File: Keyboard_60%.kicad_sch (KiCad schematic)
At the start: 24 parts, among them J3 Prog_conn, U3 NRF52833-QDAA-R7, Y1 32MHz, Y2 32.768kHz

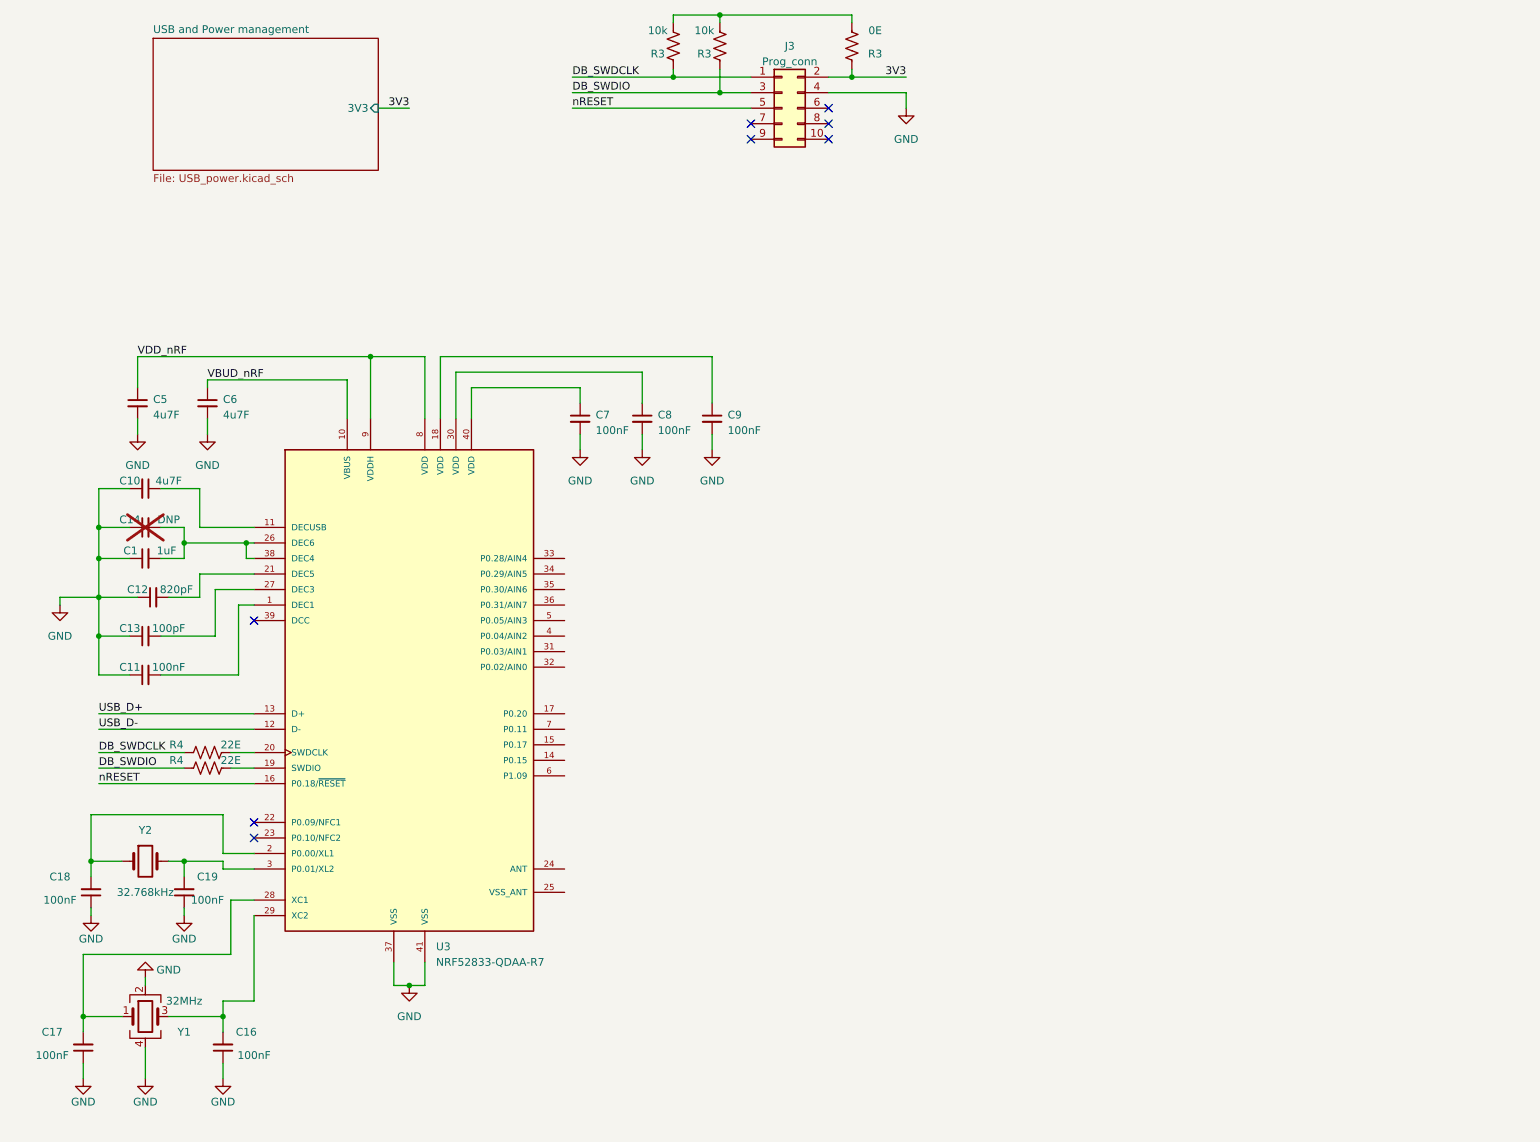
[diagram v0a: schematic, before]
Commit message: added seitch matrix to schematic
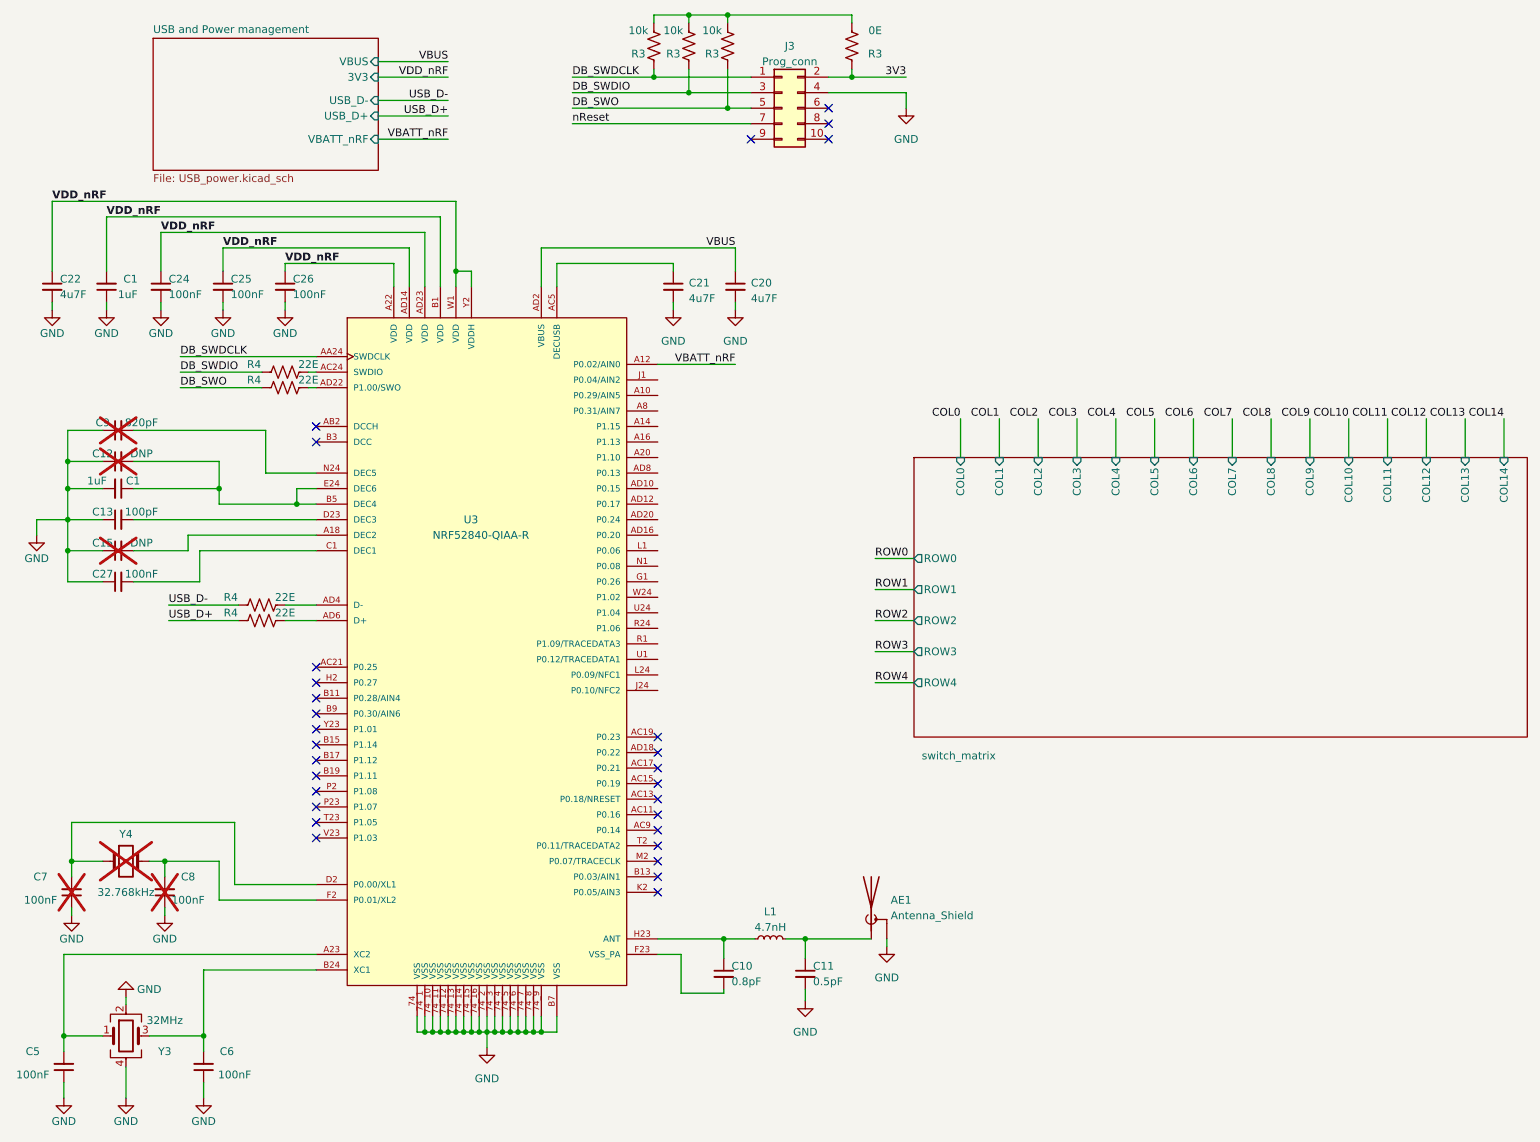
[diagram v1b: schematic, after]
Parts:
- removed C1: 1uF, symbol Device:C_Small
- removed C14: DNP, symbol keyboard:C_Small
- removed C16, C17, C18, C19: 100nF, symbol keyboard:C_Small
- removed R4 (x2): 22E, symbol keyboard:R_US
- removed U3: NRF52833-QDAA-R7, QFN40P500X500X90-41N, symbol keyboard:NRF52833-QDAA-R7
- removed Y1: 32MHz, symbol keyboard:Crystal_GND24
- removed Y2: 32.768kHz, symbol keyboard:Crystal
- added AE1: Antenna_Shield, symbol keyboard:Antenna_Shield
- added C1 (x2): 1uF, symbol Device:C_Small
- added C15: DNP, symbol keyboard:C_Small
- added C20, C21, C22: 4u7F, symbol keyboard:C_Small
- added C24, C25, C26, C27: 100nF, symbol keyboard:C_Small
- added L1: 4.7nH, symbol keyboard:L_Small
- added R3: 10k, symbol keyboard:R_US
- added R4 (x4): 22E, symbol keyboard:R_US
- added U3: NRF52840-QIAA-R, XCVR_NRF52840-QIAA-R, symbol keyboard:NRF52840-QIAA-R
- added Y3: 32MHz, symbol keyboard:Crystal_GND24
- added Y4: 32.768kHz, symbol keyboard:Crystal
- C10: value 4u7F -> 0.8pF
- C11: value 100nF -> 0.5pF
- C12: value 820pF -> DNP; now not fitted; now left out of the parts list
- C5, C6: value 4u7F -> 100nF
- C7, C8: now not fitted; now left out of the parts list
- C9: value 100nF -> 820pF; now not fitted; now left out of the parts list
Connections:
- net VBUD_nRF is gone; now on net GND: C6.1
- net DB_SWDCLK: now also U3.AA24 (SWDCLK)
- net DB_SWDIO: now also R4.1
- net GND: now also C11.2, C5.1, C7.1, C8.1, C9.1, AE1.2 (Shield), C1.1, C1.2, C15.1, C20.2, C21.2, C22.2, C24.2, C25.2, C26.2, C27.1, U3.74 (VSS), U3.74_1 (VSS), U3.74_10 (VSS), U3.74_11 (VSS), U3.74_12 (VSS), U3.74_13 (VSS), U3.74_14 (VSS), U3.74_15 (VSS), U3.74_16 (VSS), U3.74_2 (VSS), U3.74_3 (VSS), U3.74_4 (VSS), U3.74_5 (VSS), U3.74_6 (VSS), U3.74_7 (VSS), U3.74_8 (VSS), U3.74_9 (VSS), U3.B7 (VSS), Y3.2, Y3.4; no longer C10.2, C11.1, C5.2, C6.2, C7.2, C8.2, C9.2
- net USB_D+: now also R4.1
- net USB_D-: now also R4.1
- net VDD_nRF: now also C1.2, C22.1, C24.1, C25.1, C26.1, U3.A22 (VDD), U3.AD14 (VDD), U3.AD23 (VDD), U3.B1 (VDD), U3.W1 (VDD), U3.Y2 (VDDH); no longer C5.1
- net at C10.1: now also L1.1, U3.H23 (ANT)
- net at C12.2: now also C1.1, U3.B5 (DEC4), U3.E24 (DEC6)
- net at C13.2: now also U3.D23 (DEC3)
- net at R3.2, R3.2, R3.2: now also R3.2
- net nReset: now reaches J3.7 (Pin_7)
- net nRESET renamed DB_SWO
- net DB_SWO: now also R3.1, R4.1
- new net: C15.2, U3.A18 (DEC2)
- new net: AE1.1 (A), C11.1, L1.2
- new net: C7.2, U3.D2 (P0.00/XL1), Y4.1
- new net: C5.2, U3.A23 (XC2), Y3.1
- new net: C6.2, U3.B24 (XC1), Y3.3
- new net: C27.2, U3.C1 (DEC1)
- new net: R4.2, U3.AD6 (D+)
- new net: C9.2, U3.N24 (DEC5)
- new net: R4.2, U3.AC24 (SWDIO)
- new net: R4.2, U3.AD4 (D-)
- new net: C10.2, U3.F23 (VSS_PA)
- new net: C8.2, U3.F2 (P0.01/XL2), Y4.2
- new net: C21.1, U3.AC5 (DECUSB)
- new net: R4.2, U3.AD22 (P1.00/SWO)
- new net VBATT_nRF: U3.A12 (P0.02/AIN0)
- new net VBUS: C20.1, U3.AD2 (VBUS)
- no-connect marks 8 -> 29
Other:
- added sheet switch_matrix (switch_matrix.kicad_sch)
- sheet USB and Power management ports: added USB_D+, USB_D-, VBATT_nRF, VBUS; removed none
- moved on the sheet: R3
